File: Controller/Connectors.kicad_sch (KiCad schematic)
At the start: 4 parts, among them J1 UART, J2 Screw_Terminal_01x03, J3 Debug

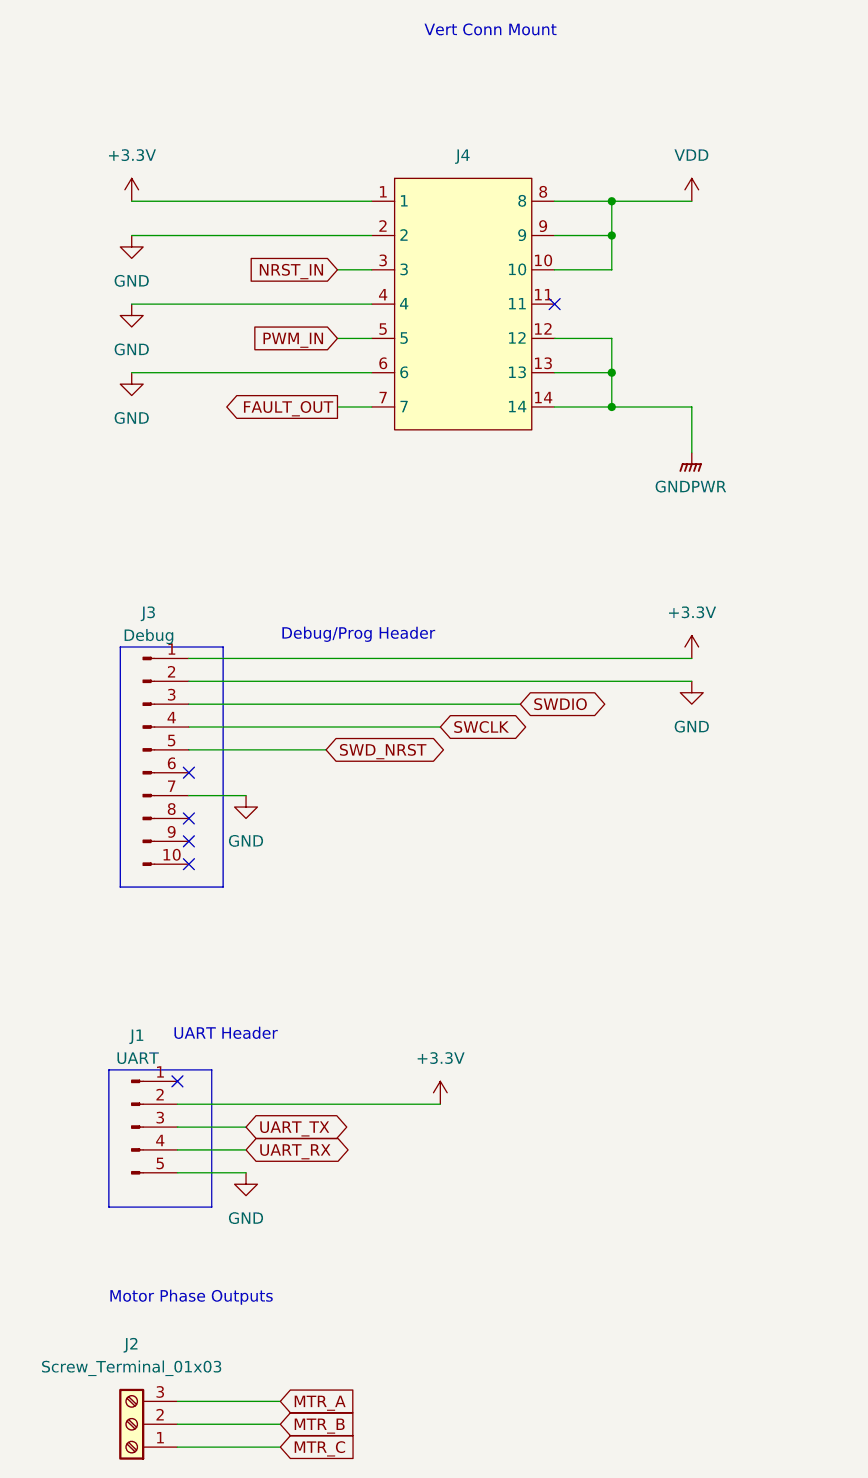
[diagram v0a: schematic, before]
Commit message: Finished Schematic for controller
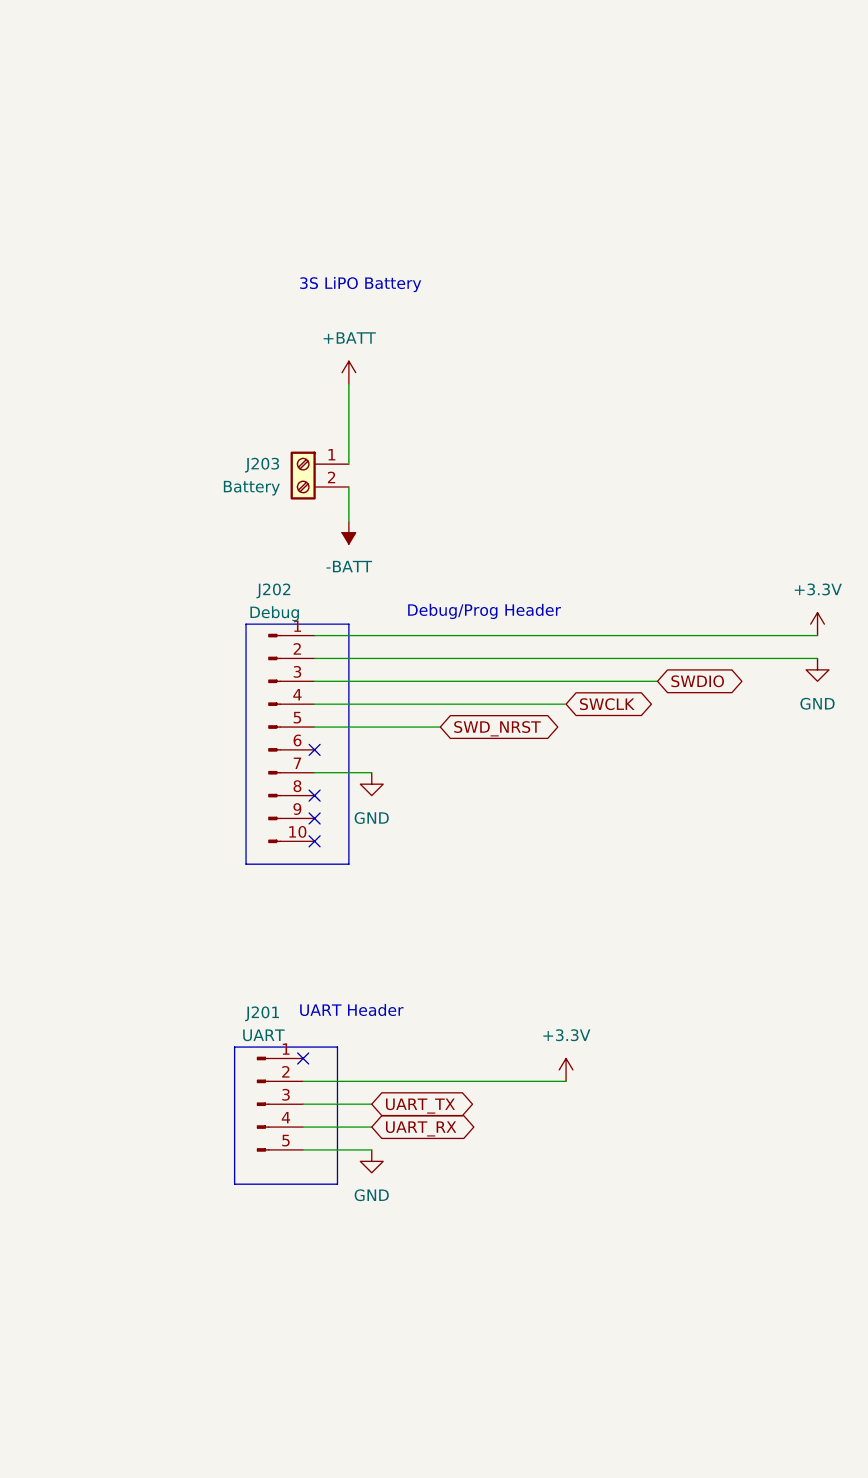
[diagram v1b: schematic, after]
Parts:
- removed J2: Screw_Terminal_01x03, Library:CUI_TB005_-762-03BE, symbol Connector:Screw_Terminal_01x03
- removed J4: ~, Library:BrushlessESC, symbol Global:BrushlessESC
- added J203: Battery, Library:CUI_TB002-500-02BE, symbol Connector:Screw_Terminal_01x02
- renumbered J1 to J201, J3 to J202
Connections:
- new net +BATT: J203.1 (Pin_1)
- new net -BATT: J203.2 (Pin_2)
- no-connect marks 6 -> 5
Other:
- note added: "3S LiPO Battery"
- note removed: "Motor Phase Outputs"
- note removed: "Vert Conn Mount"
- moved on the sheet: J201, J202
